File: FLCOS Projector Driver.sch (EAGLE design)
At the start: 77 parts, among them IC1 TLV1117LV33DCYT, IC2 MIC5323-1.8YD5-TR, IC3 MIC5504-2.5YM5-TR, IC4 TVP5150-NTSC_DECODER, IC5 CH340G, IC6 ESP32-WROOM-32UE-N4, IC7 LM3414, IC8 LM3414, IC9 LM3414, J1 MEM2075-00-140-01-A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

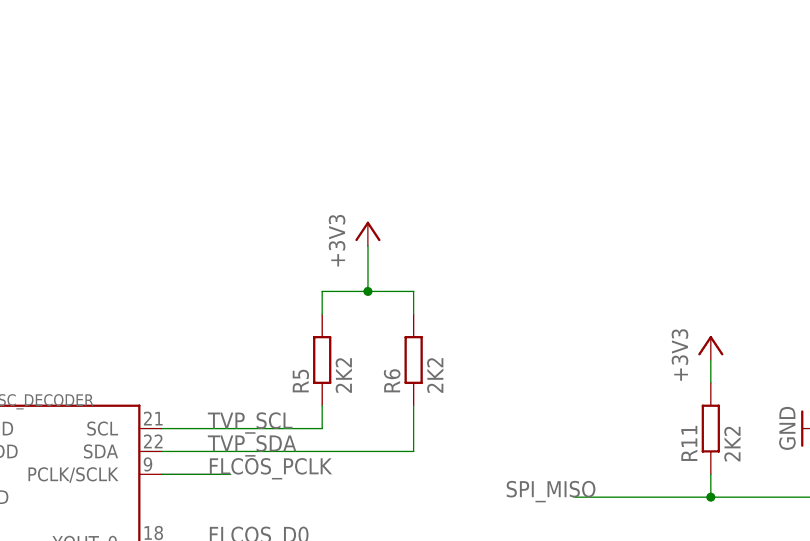
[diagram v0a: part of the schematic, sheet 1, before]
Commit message: PCB changes to fix auto-reset during Flash programming
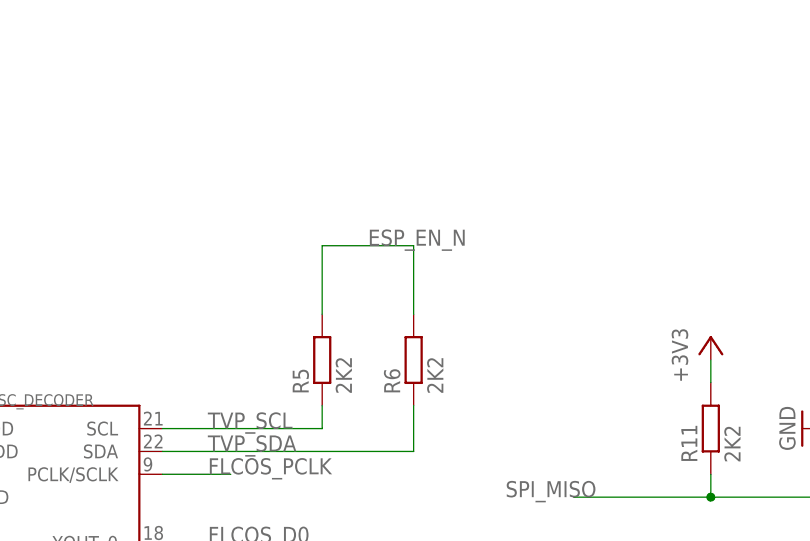
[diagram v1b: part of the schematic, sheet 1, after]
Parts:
- added R23: 2K2, rcl:R-EU_R0603
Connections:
- net +3V3: no longer R5.2, R6.2
- net ESP_EN_N: now also R5.2, R6.2
- net GND: now also R23.1
- net TVP_FL_RST_N: now also R23.2

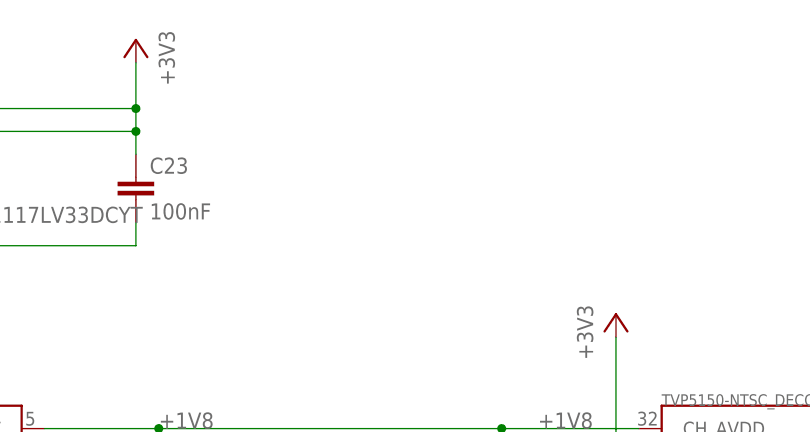
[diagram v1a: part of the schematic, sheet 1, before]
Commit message: Added JST PH fan header
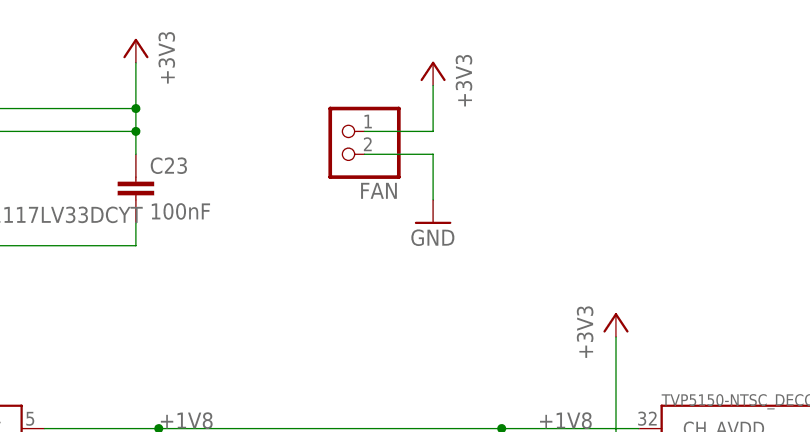
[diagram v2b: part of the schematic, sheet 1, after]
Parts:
- added FAN: (no value), adafruit:JST_2PIN-THM
- renumbered RGB to RGB_LED
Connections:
- net +3V3: now also FAN.2
- net GND: now also FAN.1
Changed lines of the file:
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@@
 <part name="P+9" library="supply1" deviceset="+5V" device=""/>
 <part name="IC1" library="SparkFun" deviceset="V_REG_LM1117" device="SOT223" value="TLV1117LV33DCYT"/>
-<part name="RGB" library="con-jst" deviceset="ZH-8" device=""/>
+<part name="RGB_LED" library="con-jst" deviceset="ZH-8" device=""/>
 <part name="L2" library="A_butts" deviceset="INDUCTOR" device="-TAIYO-YUDEN-6X2.8" value="15uH"/>
 <part name="D2" library="A_butts" deviceset="DIODE-SCHOTTKY" device="SMA" value="&quot;SB34AFC-AU_R1_000A1 SB34AFC-AU_R1_000A1&quot;"/>
@@
 <part name="R23" library="rcl" deviceset="R-EU_" device="R0603" value="2K2"/>
 <part name="GND13" library="supply1" deviceset="GND" device=""/>
+<part name="FAN" library="adafruit" deviceset="JST_2PIN" device="-THM"/>
+<part name="+3V3" library="supply1" deviceset="+3V3" device=""/>
+<part name="GND14" library="supply1" deviceset="GND" device=""/>
 </parts>
 <sheets>
@@
 <instance part="R11" gate="G$1" x="127" y="76.2" rot="R90"/>
 <instance part="+3V4" gate="G$1" x="127" y="86.36"/>
+<instance part="FAN" gate="G$1" x="2.54" y="109.22" rot="R180"/>
+<instance part="+3V3" gate="G$1" x="12.7" y="116.84" rot="MR0"/>
+<instance part="GND14" gate="1" x="12.7" y="99.06"/>
 </instances>
 <busses>
@@
 <junction x="-25.4" y="53.34"/>
 </segment>
+<segment>
+<pinref part="FAN" gate="G$1" pin="1"/>
+<pinref part="GND14" gate="1" pin="GND"/>
+<wire x1="5.08" y1="106.68" x2="12.7" y2="106.68" width="0.1524" layer="91"/>
+<wire x1="12.7" y1="106.68" x2="12.7" y2="101.6" width="0.1524" layer="91"/>
+</segment>
 </net>
 <net name="FLCOS_D7" class="0">
@@
 <pinref part="+3V4" gate="G$1" pin="+3V3"/>
 <wire x1="127" y1="81.28" x2="127" y2="83.82" width="0.1524" layer="91"/>
+</segment>
+<segment>
+<pinref part="FAN" gate="G$1" pin="2"/>
+<pinref part="+3V3" gate="G$1" pin="+3V3"/>
+<wire x1="5.08" y1="109.22" x2="12.7" y2="109.22" width="0.1524" layer="91"/>
+<wire x1="12.7" y1="109.22" x2="12.7" y2="114.3" width="0.1524" layer="91"/>
 </segment>
 </net>
@@
 </plain>
 <instances>
-<instance part="RGB" gate="G$1" x="149.86" y="66.04"/>
+<instance part="RGB_LED" gate="G$1" x="149.86" y="66.04"/>
 <instance part="L2" gate="G$1" x="76.2" y="60.96"/>
 <instance part="D2" gate="G$1" x="76.2" y="76.2" smashed="yes" rot="R90">
@@
 </segment>
 <segment>
-<pinref part="RGB" gate="G$1" pin="1"/>
+<pinref part="RGB_LED" gate="G$1" pin="1"/>
 <pinref part="P+12" gate="1" pin="+5V"/>
 <wire x1="139.7" y1="73.66" x2="137.16" y2="73.66" width="0.1524" layer="91"/>
 <wire x1="137.16" y1="73.66" x2="137.16" y2="78.74" width="0.1524" layer="91"/>
-<pinref part="RGB" gate="G$1" pin="4"/>
+<pinref part="RGB_LED" gate="G$1" pin="4"/>
 <wire x1="139.7" y1="66.04" x2="137.16" y2="66.04" width="0.1524" layer="91"/>
 <wire x1="137.16" y1="66.04" x2="137.16" y2="73.66" width="0.1524" layer="91"/>
 <junction x="137.16" y="73.66"/>
-<pinref part="RGB" gate="G$1" pin="6"/>
+<pinref part="RGB_LED" gate="G$1" pin="6"/>
 <wire x1="139.7" y1="60.96" x2="137.16" y2="60.96" width="0.1524" layer="91"/>
 <wire x1="137.16" y1="60.96" x2="137.16" y2="66.04" width="0.1524" layer="91"/>
 <junction x="137.16" y="66.04"/>
-<pinref part="RGB" gate="G$1" pin="8"/>
+<pinref part="RGB_LED" gate="G$1" pin="8"/>
 <wire x1="139.7" y1="55.88" x2="137.16" y2="55.88" width="0.1524" layer="91"/>
 <wire x1="137.16" y1="55.88" x2="137.16" y2="60.96" width="0.1524" layer="91"/>
@@
 </segment>
 <segment>
-<pinref part="RGB" gate="G$1" pin="2"/>
+<pinref part="RGB_LED" gate="G$1" pin="2"/>
 <wire x1="139.7" y1="71.12" x2="134.62" y2="71.12" width="0.1524" layer="91"/>
-<pinref part="RGB" gate="G$1" pin="3"/>
+<pinref part="RGB_LED" gate="G$1" pin="3"/>
 <wire x1="134.62" y1="71.12" x2="127" y2="71.12" width="0.1524" layer="91"/>
 <wire x1="139.7" y1="68.58" x2="134.62" y2="68.58" width="0.1524" layer="91"/>
@@
 </segment>
 <segment>
-<pinref part="RGB" gate="G$1" pin="5"/>
+<pinref part="RGB_LED" gate="G$1" pin="5"/>
 <wire x1="139.7" y1="63.5" x2="127" y2="63.5" width="0.1524" layer="91"/>
 <label x="129.54" y="63.5" size="1.778" layer="95" rot="MR0"/>
@@
 </segment>
 <segment>
-<pinref part="RGB" gate="G$1" pin="7"/>
+<pinref part="RGB_LED" gate="G$1" pin="7"/>
 <wire x1="139.7" y1="58.42" x2="127" y2="58.42" width="0.1524" layer="91"/>
 <label x="129.54" y="58.42" size="1.778" layer="95" rot="MR0"/>
